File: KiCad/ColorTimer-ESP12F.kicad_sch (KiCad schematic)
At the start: 40 parts, among them J1 SW_CON, J2 USB_B_Micro, J3 COLOER_LED, J4 AkitsukiCON, J5 GPIO_CON, J6 POWER_CON, Q1 2N7000, Q2 2N7000, SW1 RESET, SW2 Trigger SW, SW3 FLASH, SW4 SW_SPDT, U1 ESP-12F, U2 CH340K, U3 L78L33_TO92

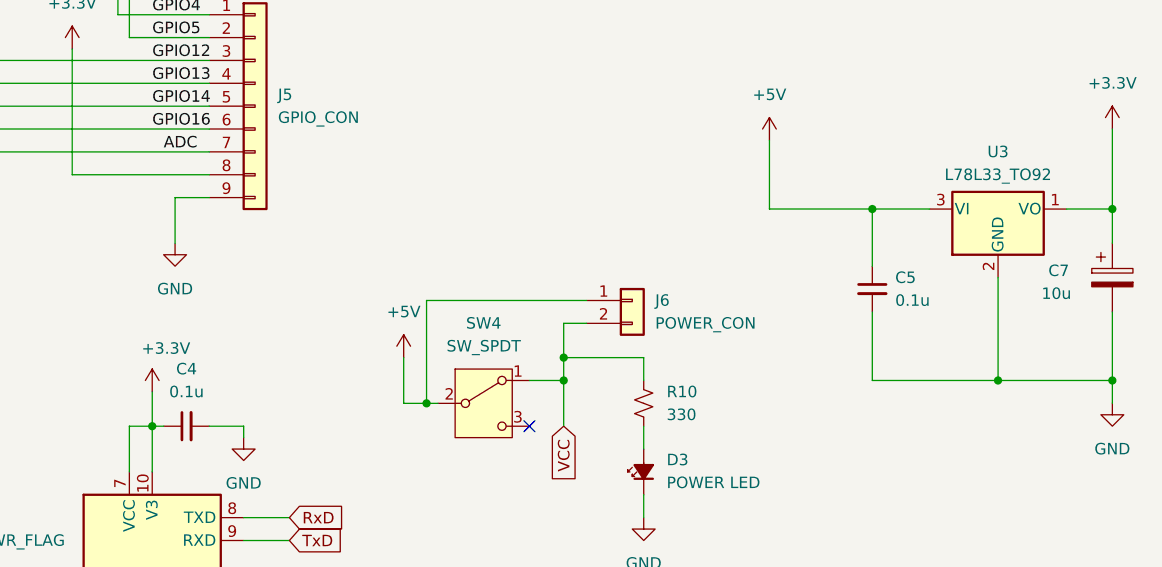
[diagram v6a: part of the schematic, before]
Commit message: コンデンサ等調整、AE-USB^MICRO-Bフットプリント追加
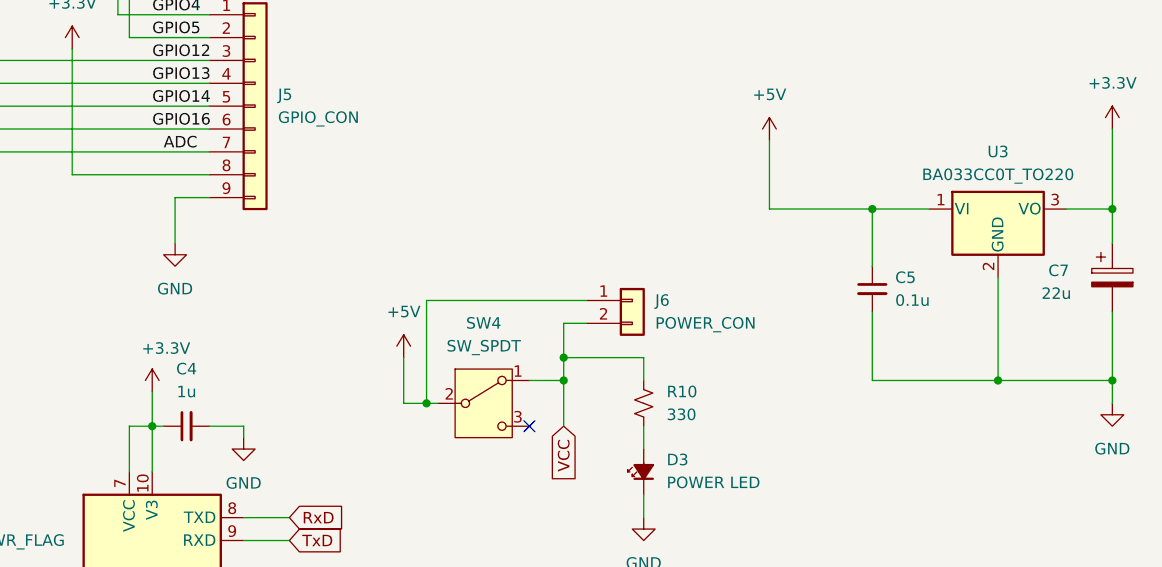
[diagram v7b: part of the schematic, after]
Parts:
- removed U3: L78L33_TO92, Package_TO_SOT_THT:TO-92_Inline_Wide, symbol Regulator_Linear:L78L33_TO92
- added U3: BA033CC0T_TO220, Package_TO_SOT_THT:TO-220-3_Vertical, symbol Regulator_Linear:LM7805_TO220
- C4: value 0.1u -> 1u
- C7: value 10u -> 22u
- J4: footprint Connector_PinSocket_2.54mm:PinSocket_1x05_P2.54mm_Vertical -> AE:AE-USB-MICRO-B-D
- Q1, Q2: footprint Package_TO_SOT_THT:TO-92_Inline -> Package_TO_SOT_THT:TO-92_Inline_Wide
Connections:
- net +3.3V: now also U3.3 (VO)
- net +5V: now also U3.1 (VI)
- net GND: now also U3.2 (GND)
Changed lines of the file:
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@@
+	)
+	(symbol
+		(lib_id "Regulator_Linear:LM7805_TO220")
+		(at 240.03 111.76 0)
+		(unit 1)
+		(exclude_from_sim no)
+		(in_bom yes)
+		(on_board yes)
+		(dnp no)
+		(fields_autoplaced yes)
+		(property "Reference" "U3"
+			(at 240.03 105.41 0)
+			(effects
+				(font
+					(size 1.27 1.27)
+				)
+			)
+		)
+		(property "Value" "BA033CC0T_TO220"
+			(at 240.03 107.95 0)
+			(effects
+				(font
+					(size 1.27 1.27)
+				)
+			)
+		)
+		(property "Footprint" "Package_TO_SOT_THT:TO-220-3_Vertical"
+			(at 240.03 106.045 0)
+			(effects
+				(font
+					(size 1.27 1.27)
+					(italic yes)
+				)
+				(hide yes)
+			)
+		)
+		(property "Datasheet" "https://www.onsemi.cn/PowerSolutions/document/MC7800-D.PDF"
+			(at 240.03 113.03 0)
+			(effects
+				(font
+					(size 1.27 1.27)
+				)
+				(hide yes)
+			)
+		)
+		(property "Description" "Positive 1A 35V Linear Regulator, Fixed Output 5V, TO-220"
+			(at 240.03 111.76 0)
+			(effects
+				(font
+					(size 1.27 1.27)
+				)
+				(hide yes)
+			)
+		)
+		(pin "1"
+		)
+		(pin "3"
+		)
+		(pin "2"
+		)
+		(instances
+			(project ""
+				(path "/3ff58839-42d9-41e5-8791-30721827b8bc"
+					(reference "U3")
+					(unit 1)
+				)
+			)
+		)
 	)
 	(symbol
@@
 			)
 		)
-		(property "Value" "0.1u"
+		(property "Value" "1u"
 			(at 149.8663 132.08 90)
 			(effects
@@
 	)
 	(symbol
-		(lib_id "Regulator_Linear:L78L33_TO92")
-		(at 240.03 111.76 0)
-		(unit 1)
-		(exclude_from_sim no)
-		(in_bom yes)
-		(on_board yes)
-		(dnp no)
-		(fields_autoplaced yes)
-		(property "Reference" "U3"
-			(at 240.03 105.41 0)
-			(effects
-				(font
-					(size 1.27 1.27)
-				)
-			)
-		)
-		(property "Value" "L78L33_TO92"
-			(at 240.03 107.95 0)
-			(effects
-				(font
-					(size 1.27 1.27)
-				)
-			)
-		)
-		(property "Footprint" "Package_TO_SOT_THT:TO-92_Inline_Wide"
-			(at 240.03 106.045 0)
-			(effects
-				(font
-					(size 1.27 1.27)
-					(italic yes)
-				)
-				(hide yes)
-			)
-		)
-		(property "Datasheet" "http://www.st.com/content/ccc/resource/technical/document/datasheet/15/55/e5/aa/23/5b/43/fd/CD00000446.pdf/files/CD00000446.pdf/jcr:content/translations/en.CD00000446.pdf"
-			(at 240.03 113.03 0)
-			(effects
-				(font
-					(size 1.27 1.27)
-				)
-				(hide yes)
-			)
-		)
-		(property "Description" "Positive 100mA 30V Linear Regulator, Fixed Output 3.3V, TO-92"
-			(at 240.03 111.76 0)
-			(effects
-				(font
-					(size 1.27 1.27)
-				)
-				(hide yes)
-			)
-		)
-		(pin "3"
-		)
-		(pin "2"
-		)
-		(pin "1"
-		)
-		(instances
-			(project ""
-				(path "/3ff58839-42d9-41e5-8791-30721827b8bc"
-					(reference "U3")
-					(unit 1)
-				)
-			)
-		)
-	)
-	(symbol
 		(lib_id "Device:R_Small_US")
 		(at 200.66 133.35 180)
@@
 			)
 		)
-		(property "Footprint" "Connector_PinSocket_2.54mm:PinSocket_1x05_P2.54mm_Vertical"
+		(property "Footprint" "AE:AE-USB-MICRO-B-D"
 			(at 134.62 182.88 0)
 			(effects
@@
 			)
 		)
-		(property "Footprint" "Package_TO_SOT_THT:TO-92_Inline"
+		(property "Footprint" "Package_TO_SOT_THT:TO-92_Inline_Wide"
 			(at 218.44 48.895 0)
 			(effects
@@
 			)
 		)
-		(property "Footprint" "Package_TO_SOT_THT:TO-92_Inline"
+		(property "Footprint" "Package_TO_SOT_THT:TO-92_Inline_Wide"
 			(at 218.44 62.865 0)
 			(effects
@@
 			)
 		)
-		(property "Value" "10u"
+		(property "Value" "22u"
 			(at 244.856 121.158 0)
 			(effects

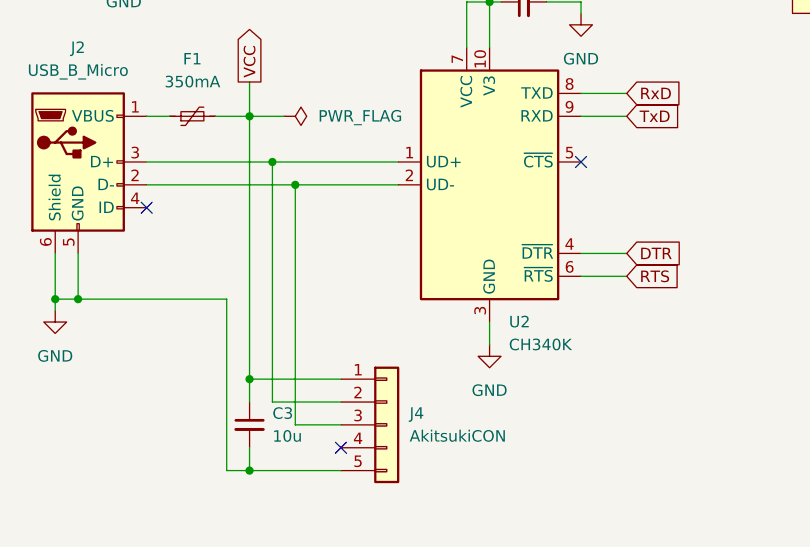
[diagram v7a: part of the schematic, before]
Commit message: 回路間違い修正 & ガーバー出力
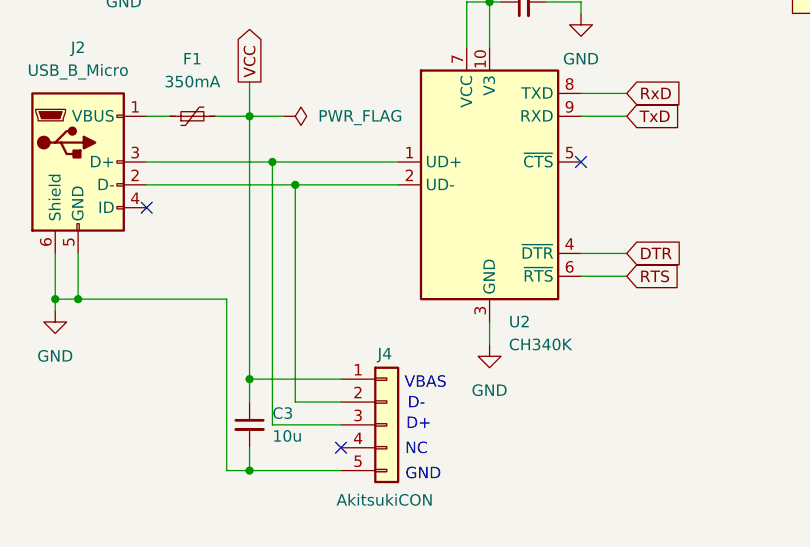
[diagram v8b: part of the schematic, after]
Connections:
- net at J2.3 (D+), U2.1 (UD+): now also J4.3 (Pin_3); no longer J4.2 (Pin_2)
- net at J2.2 (D-), U2.2 (UD-): now also J4.2 (Pin_2); no longer J4.3 (Pin_3)
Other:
- note added: "D+"
- note added: "D-"
- note added: "GND"
- note added: "NC"
- note added: "VBAS"
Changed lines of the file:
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@@
 		(comment 4 "ESP-12FモジュールにCH340K経由のシリアル書き込み回路を追加したもの")
 	)
+	(text "GND"
+		(exclude_from_sim no)
+		(at 138.684 188.468 0)
+		(effects
+			(font
+				(size 1.27 1.27)
+			)
+		)
+	)
+	(text "D-"
+		(exclude_from_sim no)
+		(at 137.922 180.594 0)
+		(effects
+			(font
+				(size 1.27 1.27)
+			)
+		)
+	)
+	(text "NC"
+		(exclude_from_sim no)
+		(at 137.922 185.674 0)
+		(effects
+			(font
+				(size 1.27 1.27)
+			)
+		)
+	)
+	(text "D+"
+		(exclude_from_sim no)
+		(at 138.176 182.88 0)
+		(effects
+			(font
+				(size 1.27 1.27)
+			)
+		)
+	)
+	(text "VBAS"
+		(exclude_from_sim no)
+		(at 138.938 178.308 0)
+		(effects
+			(font
+				(size 1.27 1.27)
+			)
+		)
+	)
 	(junction
 		(at 91.44 95.25)
@@
 	(wire
 		(pts
+			(xy 121.92 153.67) (xy 121.92 182.88)
+		)
+		(stroke
+			(width 0)
+			(type default)
+		)
+	)
+	(wire
+		(pts
 			(xy 93.98 52.07) (xy 76.2 52.07)
 		)
@@
 	(wire
 		(pts
-			(xy 124.46 156.21) (xy 124.46 182.88)
+			(xy 124.46 156.21) (xy 124.46 180.34)
 		)
 		(stroke
@@
 	(wire
 		(pts
-			(xy 121.92 153.67) (xy 121.92 180.34)
-		)
-		(stroke
-			(width 0)
-			(type default)
-		)
-	)
-	(wire
-		(pts
 			(xy 149.86 57.15) (xy 160.02 57.15)
 		)
@@
 	(wire
 		(pts
-			(xy 121.92 180.34) (xy 129.54 180.34)
-		)
-		(stroke
-			(width 0)
-			(type default)
-		)
-	)
-	(wire
-		(pts
 			(xy 104.14 86.36) (xy 140.97 86.36)
 		)
@@
 	(wire
 		(pts
-			(xy 124.46 182.88) (xy 129.54 182.88)
-		)
-		(stroke
-			(width 0)
-			(type default)
-		)
-	)
-	(wire
-		(pts
 			(xy 93.98 62.23) (xy 88.9 62.23)
 		)
@@
 	(wire
 		(pts
+			(xy 121.92 182.88) (xy 129.54 182.88)
+		)
+		(stroke
+			(width 0)
+			(type default)
+		)
+	)
+	(wire
+		(pts
 			(xy 139.7 59.69) (xy 157.48 59.69)
 		)
@@
 	(wire
 		(pts
+			(xy 124.46 180.34) (xy 129.54 180.34)
+		)
+		(stroke
+			(width 0)
+			(type default)
+		)
+	)
+	(wire
+		(pts
 			(xy 187.96 130.81) (xy 191.77 130.81)
 		)
@@
 		(on_board yes)
 		(dnp no)
-		(fields_autoplaced yes)
 		(property "Reference" "J4"
-			(at 137.16 181.6099 0)
+			(at 133.604 175.006 0)
 			(effects
 				(font
@@
 		)
 		(property "Value" "AkitsukiCON"
-			(at 137.16 184.1499 0)
+			(at 129.032 191.262 0)
 			(effects
 				(font
